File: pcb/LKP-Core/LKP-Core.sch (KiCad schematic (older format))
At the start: 4 parts

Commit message: LKP-Core WIP
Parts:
- added C? (x5): 1uF, symbol Device:C_Small
- added C? (x4): 0.1uF, symbol Device:C_Small
- added J?: SWD, symbol Connector:Conn_01x05_Male
- added J?: Intercon L, symbol Connector_Generic:Conn_02x09_Odd_Even
- added J?: Intercon R, symbol Connector_Generic:Conn_02x09_Odd_Even
- added RN?: R_Pack04, symbol Device:R_Pack04
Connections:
- net +5V: now also J?.1 (Pin_1)
- net VDD: now reaches U?.11 (VDDA)
- net VDD: now also FB?.2, U?.26 (VDDIO), U?.50 (VDDD), U?.56 (VDDA), C?.1, C?.1, C?.1, C?.1, C?.1, C?.1, C?.1, C?.1
- net INT: now reaches U?.18 (P3.0)
- net LED: now reaches U?.19 (P3.1)
- net S0_0: now reaches U?.22 (P3.4)
- net S0_0: now also RN?.1 (R1.1)
- net S0_1: now reaches U?.23 (P3.5)
- net S0_1: now also RN?.2 (R2.1)
- net S0_2: now reaches U?.24 (P3.6)
- net S0_2: now also RN?.3 (R3.1)
- net S0_3: now reaches U?.25 (P3.7)
- net S0_3: now also RN?.4 (R4.1)
- net CMOD: now reaches U?.29 (P4.2)
- net CMOD: now also C?.1
- net CSH: now reaches U?.30 (P4.3)
- net CSH: now also C?.1
- net at U?.48 (VCCD): now also C?.2
- net LED_STAT: now reaches U?.64 (P1.6)
- net GND: now reaches C?.2
- net GND: now also C?.2, C?.1, C?.2, C?.2, C?.2, C?.2, C?.2, C?.2, C?.2, C?.2, J?.2 (Pin_2)
- new net E0_0: J?.2 (Pin_2), RN?.8 (R1.2)
- new net E0_1: J?.3 (Pin_3), RN?.7 (R2.2)
- new net E0_2: J?.4 (Pin_4), RN?.6 (R3.2)
- new net E0_3: J?.5 (Pin_5), RN?.5 (R4.2)
- new net E0_4: J?.6 (Pin_6)
- new net E0_5: J?.7 (Pin_7)
- new net RESET: J?.3 (Pin_3)
- new net SWCLK: J?.4 (Pin_4)
- new net SWDIO: J?.5 (Pin_5)
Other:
- moved on the sheet: C?, FB?

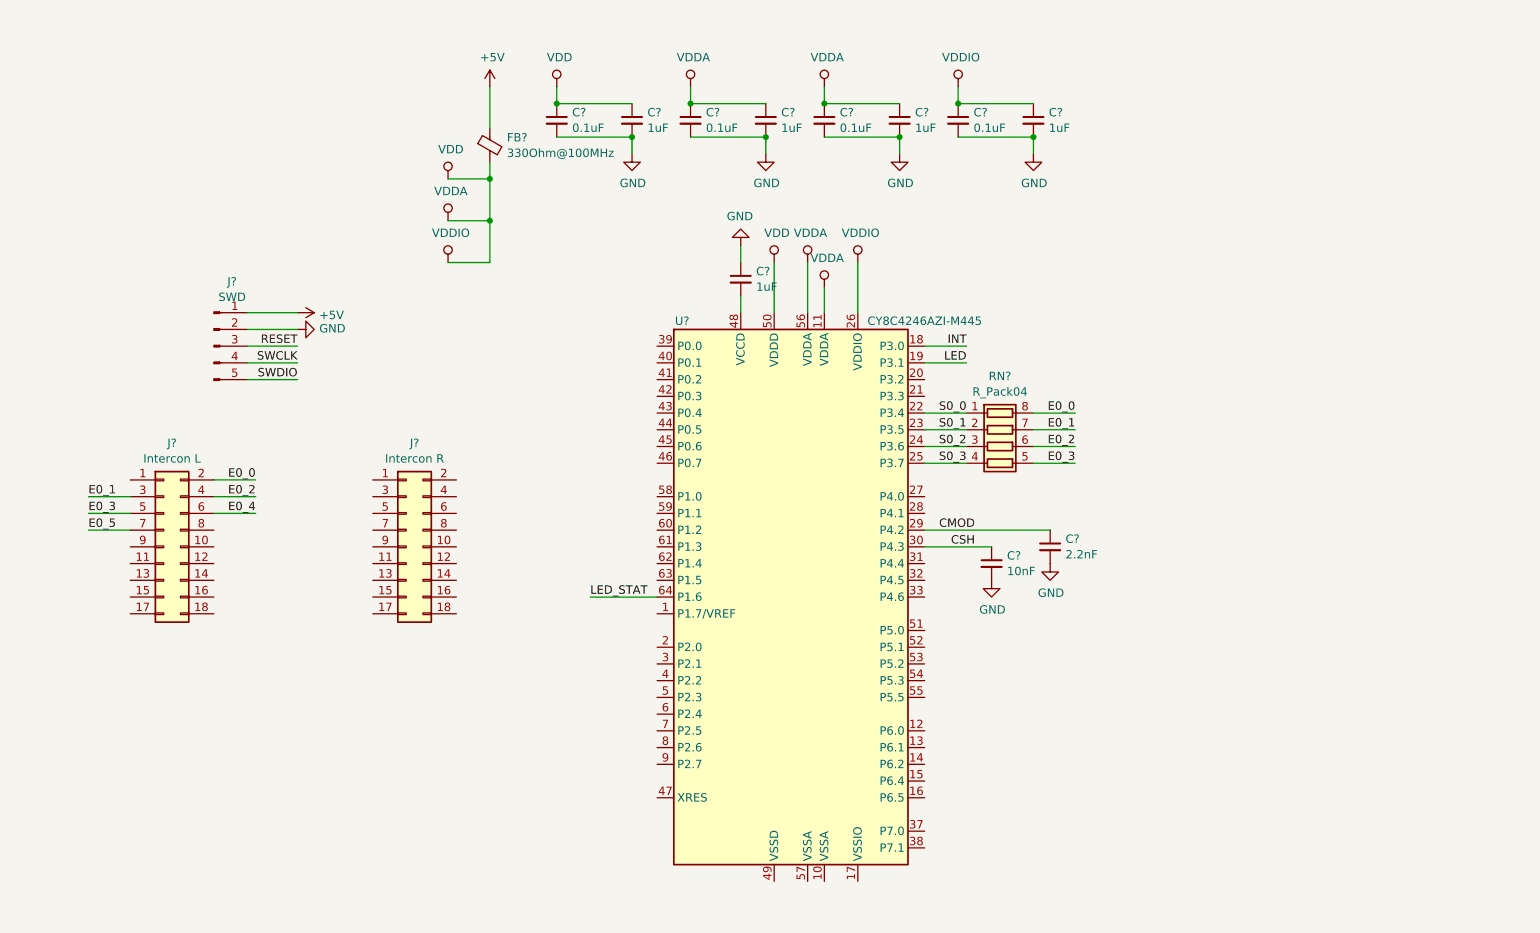
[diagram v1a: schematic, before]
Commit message: Finish schematic
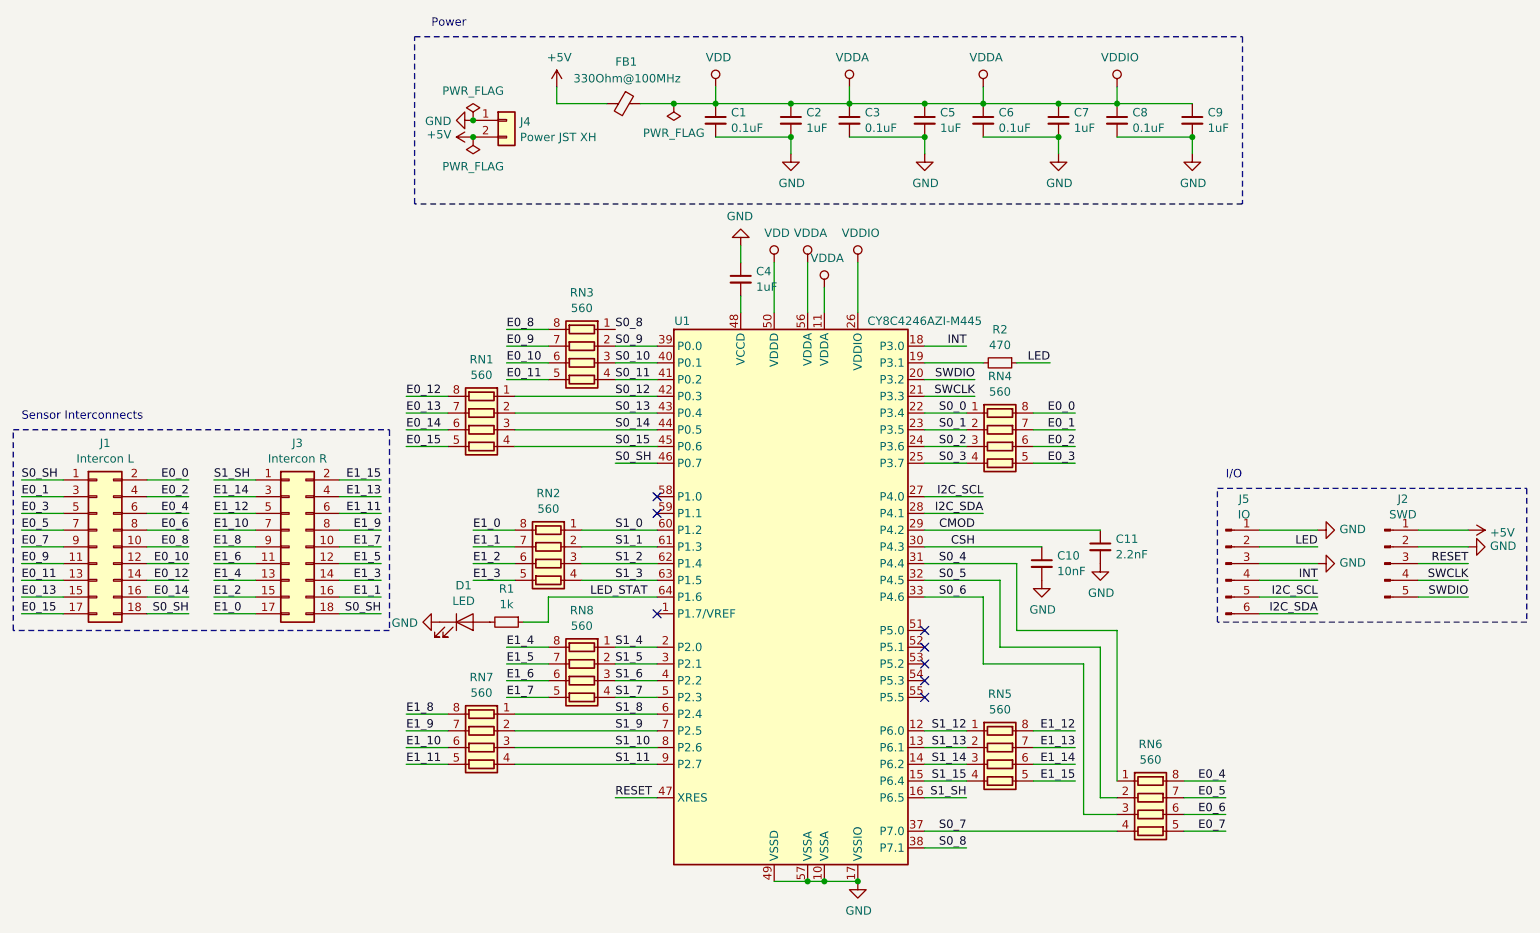
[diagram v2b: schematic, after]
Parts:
- added D1: LED, symbol Device:LED
- added J4: Power JST XH, symbol Connector_Generic:Conn_01x02
- added J5: IO, symbol Connector:Conn_01x06_Male
- added R1: 1k, symbol Device:R_Small
- added R2: 470, symbol Device:R_Small
- added RN1, RN2, RN3, RN5, RN6, RN7, RN8: 560, symbol Device:R_Pack04
- RN4: renamed from RN?; value R_Pack04 -> 560
- gave numbers to parts that had none: 16
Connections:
- net +5V: now also FB1.2, J4.2 (Pin_2); no longer FB1.1
- net E0_4: now also RN6.8 (R1.2)
- net E0_5: now also RN6.7 (R2.2)
- net GND: now also U1.10 (VSSA), U1.17 (VSSIO), U1.49 (VSSD), U1.57 (VSSA), D1.1 (K), J4.1 (Pin_1), J5.1 (Pin_1), J5.3 (Pin_3)
- net INT: now also J5.4 (Pin_4)
- net LED: now also J5.2 (Pin_2), R2.1; no longer U1.19 (P3.1)
- net LED_STAT: now also R1.1
- net RESET: now also U1.47 (XRES)
- net SWCLK: now also U1.21 (P3.3)
- net SWDIO: now also U1.20 (P3.2)
- net VDD: now also FB1.1; no longer FB1.2
- net S1_12: now reaches U1.12 (P6.0)
- net S1_12: now also RN5.1 (R1.1)
- net S1_13: now reaches U1.13 (P6.1)
- net S1_13: now also RN5.2 (R2.1)
- net S1_14: now reaches U1.14 (P6.2)
- net S1_14: now also RN5.3 (R3.1)
- net S1_15: now reaches U1.15 (P6.4)
- net S1_15: now also RN5.4 (R4.1)
- net S1_SH: now reaches U1.16 (P6.5)
- net S1_SH: now also J3.1 (Pin_1)
- net S1_4: now reaches U1.2 (P2.0)
- net S1_4: now also RN8.1 (R1.1)
- net I2C_SCL: now reaches U1.27 (P4.0)
- net I2C_SCL: now also J5.5 (Pin_5)
- net I2C_SDA: now reaches U1.28 (P4.1)
- net I2C_SDA: now also J5.6 (Pin_6)
- net S1_5: now reaches U1.3 (P2.1)
- net S1_5: now also RN8.2 (R2.1)
- net S0_4: now reaches U1.31 (P4.4)
- net S0_4: now also RN6.1 (R1.1)
- net S0_5: now reaches U1.32 (P4.5)
- net S0_5: now also RN6.2 (R2.1)
- net S0_6: now reaches U1.33 (P4.6)
- net S0_6: now also RN6.3 (R3.1)
- net S0_7: now reaches U1.37 (P7.0)
- net S0_7: now also RN6.4 (R4.1)
- net S0_8: now reaches U1.38 (P7.1)
- net S0_8: now also RN3.1 (R1.1)
- net S0_9: now reaches U1.39 (P0.0)
- net S0_9: now also RN3.2 (R2.1)
- net S1_6: now reaches U1.4 (P2.2)
- net S1_6: now also RN8.3 (R3.1)
- net S0_10: now reaches U1.40 (P0.1)
- net S0_10: now also RN3.3 (R3.1)
- net S0_11: now reaches U1.41 (P0.2)
- net S0_11: now also RN3.4 (R4.1)
- net S0_12: now reaches U1.42 (P0.3)
- net S0_12: now also RN1.1 (R1.1)
- net S0_13: now reaches U1.43 (P0.4)
- net S0_13: now also RN1.2 (R2.1)
- net S0_14: now reaches U1.44 (P0.5)
- net S0_14: now also RN1.3 (R3.1)
- net S0_15: now reaches U1.45 (P0.6)
- net S0_15: now also RN1.4 (R4.1)
- net S0_SH: now reaches U1.46 (P0.7)
- net S0_SH: now also J1.1 (Pin_1), J1.18 (Pin_18), J3.18 (Pin_18)
- net S1_7: now reaches U1.5 (P2.3)
- net S1_7: now also RN8.4 (R4.1)
- net S1_8: now reaches U1.6 (P2.4)
- net S1_8: now also RN7.1 (R1.1)
- net S1_0: now reaches U1.60 (P1.2)
- net S1_0: now also RN2.1 (R1.1)
- net S1_1: now reaches U1.61 (P1.3)
- net S1_1: now also RN2.2 (R2.1)
- net S1_2: now reaches U1.62 (P1.4)
- net S1_2: now also RN2.3 (R3.1)
- net S1_3: now reaches U1.63 (P1.5)
- net S1_3: now also RN2.4 (R4.1)
- net S1_9: now reaches U1.7 (P2.5)
- net S1_9: now also RN7.2 (R2.1)
- net S1_10: now reaches U1.8 (P2.6)
- net S1_10: now also RN7.3 (R3.1)
- net S1_11: now reaches U1.9 (P2.7)
- net S1_11: now also RN7.4 (R4.1)
- net E0_8: now reaches J1.10 (Pin_10)
- net E0_8: now also RN3.8 (R1.2)
- net E0_9: now reaches J1.11 (Pin_11)
- net E0_9: now also RN3.7 (R2.2)
- net E0_10: now reaches J1.12 (Pin_12)
- net E0_10: now also RN3.6 (R3.2)
- net E0_11: now reaches J1.13 (Pin_13)
- net E0_11: now also RN3.5 (R4.2)
- net E0_12: now reaches J1.14 (Pin_14)
- net E0_12: now also RN1.8 (R1.2)
- net E0_13: now reaches J1.15 (Pin_15)
- net E0_13: now also RN1.7 (R2.2)
- net E0_14: now reaches J1.16 (Pin_16)
- net E0_14: now also RN1.6 (R3.2)
- net E0_15: now reaches J1.17 (Pin_17)
- net E0_15: now also RN1.5 (R4.2)
- net E0_6: now reaches J1.8 (Pin_8)
- net E0_6: now also RN6.6 (R3.2)
- net E0_7: now reaches J1.9 (Pin_9)
- net E0_7: now also RN6.5 (R4.2)
- net E1_7: now reaches J3.10 (Pin_10)
- net E1_7: now also RN8.5 (R4.2)
- net E1_6: now reaches J3.11 (Pin_11)
- net E1_6: now also RN8.6 (R3.2)
- net E1_5: now reaches J3.12 (Pin_12)
- net E1_5: now also RN8.7 (R2.2)
- net E1_4: now reaches J3.13 (Pin_13)
- net E1_4: now also RN8.8 (R1.2)
- net E1_3: now reaches J3.14 (Pin_14)
- net E1_3: now also RN2.5 (R4.2)
- net E1_2: now reaches J3.15 (Pin_15)
- net E1_2: now also RN2.6 (R3.2)
- net E1_1: now reaches J3.16 (Pin_16)
- net E1_1: now also RN2.7 (R2.2)
- net E1_0: now reaches J3.17 (Pin_17)
- net E1_0: now also RN2.8 (R1.2)
- net E1_15: now reaches J3.2 (Pin_2)
- net E1_15: now also RN5.5 (R4.2)
- net E1_14: now reaches J3.3 (Pin_3)
- net E1_14: now also RN5.6 (R3.2)
- net E1_13: now reaches J3.4 (Pin_4)
- net E1_13: now also RN5.7 (R2.2)
- net E1_12: now reaches J3.5 (Pin_5)
- net E1_12: now also RN5.8 (R1.2)
- net E1_11: now reaches J3.6 (Pin_6)
- net E1_11: now also RN7.5 (R4.2)
- net E1_10: now reaches J3.7 (Pin_7)
- net E1_10: now also RN7.6 (R3.2)
- net E1_9: now reaches J3.8 (Pin_8)
- net E1_9: now also RN7.7 (R2.2)
- net E1_8: now reaches J3.9 (Pin_9)
- net E1_8: now also RN7.8 (R1.2)
- new net: R2.2, U1.19 (P3.1)
- new net: D1.2 (A), R1.2
- no-connect marks 0 -> 8
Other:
- note added: "I/O"
- note added: "Power"
- note added: "Sensor Interconnects"
- moved on the sheet: C1, C10, C11, C2, C3, C5, C6, C7, C8, C9, FB1, J1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

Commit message: Misc changes to schematic
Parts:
- added D2: MBR0520L, symbol Device:D_Schottky_Small
- U1: footprint (none) -> Package_QFP:TQFP-64_10x10mm_P0.5mm
- renumbered C8 to C10, C9 to C11, C4 to C2, C2 to C3, C3 to C4, C10 to C7, C7 to C8, C11 to C9, J3 to J2, J4 to J3, J5 to J4, J2 to J5, RN7 to RN2, RN2 to RN3, RN3 to RN4, RN8 to RN5, RN4 to RN6, RN5 to RN7, RN6 to RN8
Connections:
- net +5V: now also D2.1 (K); no longer J3.2 (Pin_2)
- net GND: now also C2.2; no longer C2.1
- net at U1.48 (VCCD): now also C2.1; no longer C2.2
- new net: D2.2 (A), J3.2 (Pin_2)
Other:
- moved on the sheet: J3
